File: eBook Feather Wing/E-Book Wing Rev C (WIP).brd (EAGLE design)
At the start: 77.5 x 112.3 mm, 100 parts, among them IC1 MCP23008/SO, IC2 23K256-I/SN, J1 MJ-3523-SMT, Q1 IRLML0100, SW1 SPDT_SWITCH

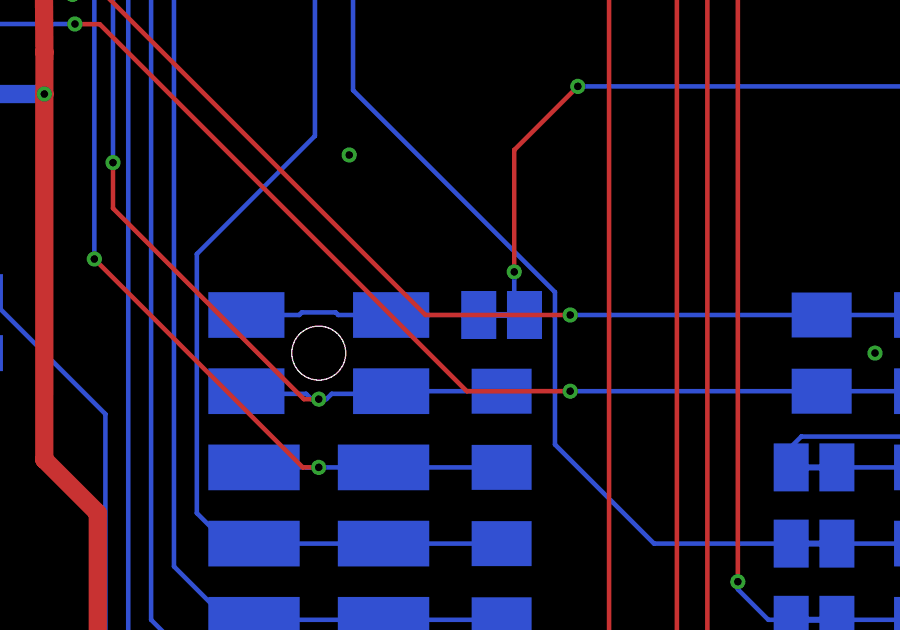
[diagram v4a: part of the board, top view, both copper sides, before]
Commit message: make the FCS jumper open by default
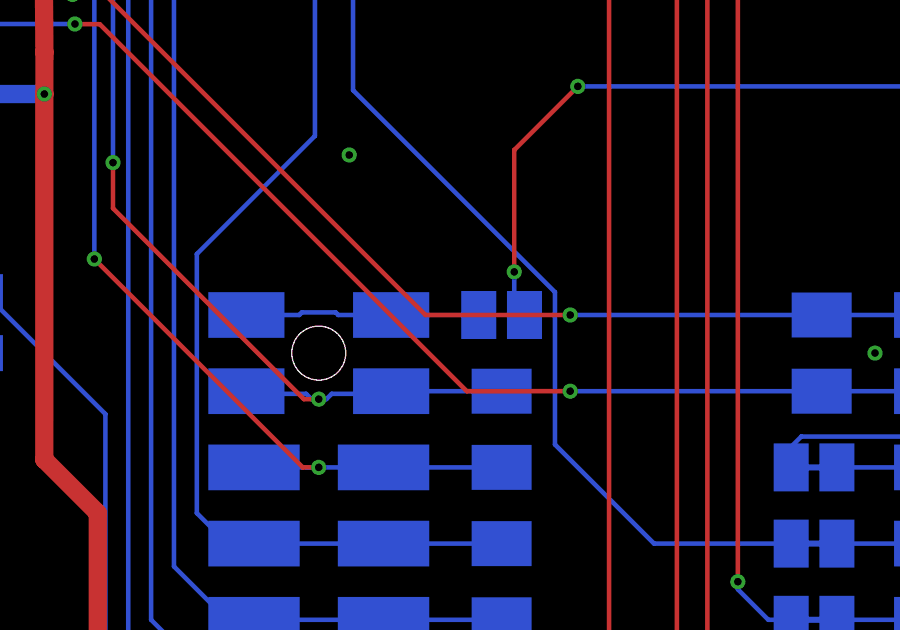
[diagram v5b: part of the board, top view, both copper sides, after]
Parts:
- FCS: value (none) -> SOLDERJUMPER_OPEN; device Adafruit 3.5in 480x320 FeatherWing:MICROBUILDER_SOLDERJUMPER_CLOSEDWIRE -> E-Book Wing Rev C (WIP):SOLDERJUMPER_OPEN
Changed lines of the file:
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@@
 <?xml version="1.0" encoding="utf-8"?>
 <!DOCTYPE eagle SYSTEM "eagle.dtd">
-<eagle version="9.4.2">
+<eagle version="9.5.1">
 <drawing>
 <settings>
@@
 <layer number="27" name="tValues" color="7" fill="1" visible="no" active="yes"/>
 <layer number="28" name="bValues" color="7" fill="1" visible="no" active="yes"/>
-<layer number="29" name="tStop" color="7" fill="3" visible="yes" active="yes"/>
+<layer number="29" name="tStop" color="7" fill="3" visible="no" active="yes"/>
 <layer number="30" name="bStop" color="7" fill="6" visible="no" active="yes"/>
 <layer number="31" name="tCream" color="7" fill="4" visible="no" active="yes"/>
@@
 <attribute name="NAME" x="58.674" y="7.747" size="0.8128" layer="52" font="vector" ratio="18" rot="MR0" align="center"/>
 </element>
-<element name="FCS" library="Adafruit 3.5in 480x320 FeatherWing" package="MICROBUILDER_SOLDERJUMPER_CLOSEDWIRE" value="" x="33.274" y="44.45" smashed="yes" rot="MR180">
-<attribute name="NAME" x="35.56" y="44.45" size="0.508" layer="26" font="vector" ratio="18" rot="MR90" align="center"/>
-<attribute name="VALUE" x="31.75" y="46.101" size="0.4064" layer="28" ratio="10" rot="MR180"/>
-</element>
 <element name="U$48" library="My Stuff" package="OSO_ONELINE_125MIL" value="OSO_TEXTOSO_TEXT_ONELINE_125MIL" x="45.339" y="14.732" smashed="yes"/>
 <element name="U$44" library="My Stuff" package="OSO_GRAPHIC" value="OSO_GRAPHIC" x="3.81" y="13.081" smashed="yes"/>
 <element name="U$45" library="My Stuff" package="OSO_BEAR_750MIL" value="OSO_BEAR" x="61.976" y="27.178" smashed="yes"/>
+<element name="FCS" library="E-Book Wing Rev C (WIP)" package="SOLDERJUMPER_OPEN" value="SOLDERJUMPER_OPEN" x="33.274" y="44.45" smashed="yes" rot="MR180">
+<attribute name="NAME" x="35.56" y="44.45" size="0.508" layer="26" font="vector" ratio="18" rot="MR90" align="center"/>
+<attribute name="VALUE" x="31.75" y="46.101" size="0.4064" layer="28" ratio="10" rot="MR180"/>
+</element>
 </elements>
 <signals>
@@
 <wire x1="27.827375" y1="44.45" x2="29.591" y2="44.45" width="0.1524" layer="16"/>
 <contactref element="FCS" pad="1"/>
-<wire x1="29.591" y1="44.45" x2="32.512" y2="44.45" width="0.1524" layer="16"/>
+<wire x1="32.512" y1="44.45" x2="29.591" y2="44.45" width="0.1524" layer="16"/>
 </signal>
 <signal name="+3V3">
@@
 <signal name="FLASH_CS">
 <contactref element="IC3" pad="1"/>
-<contactref element="FCS" pad="2"/>
-<wire x1="34.036" y1="44.45" x2="33.69475" y2="44.79125" width="0.1524" layer="16"/>
 <wire x1="33.69475" y1="44.79125" x2="33.69475" y2="45.88675" width="0.1524" layer="16"/>
 <via x="33.69475" y="45.88675" extent="1-16" drill="0.254"/>
@@
 <wire x1="53.34" y1="54.61" x2="52.705" y2="55.245" width="0.1524" layer="16"/>
 <wire x1="52.705" y1="55.245" x2="52.705" y2="56.074" width="0.1524" layer="16"/>
+<contactref element="FCS" pad="2"/>
+<wire x1="34.036" y1="44.45" x2="33.69475" y2="44.79125" width="0.1524" layer="16"/>
 </signal>
 <signal name="GPIO_INT">
